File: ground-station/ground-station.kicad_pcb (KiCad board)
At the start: 2 copper layers, 61.6 x 32.6 mm, 53 parts, among them J1 Conn_01x02, J10 Conn_01x02, J2 Conn_01x02, J3 Conn_01x02, J4 Conn_01x02, J5 Conn_01x05, J6 Conn_01x04, J7 USB_B_Micro, J8 Conn_01x02, J9 Conn_01x02, SW1 SW_Push, U1 LM3940, U2 STM32F401RETx, U3 RFM69HCW

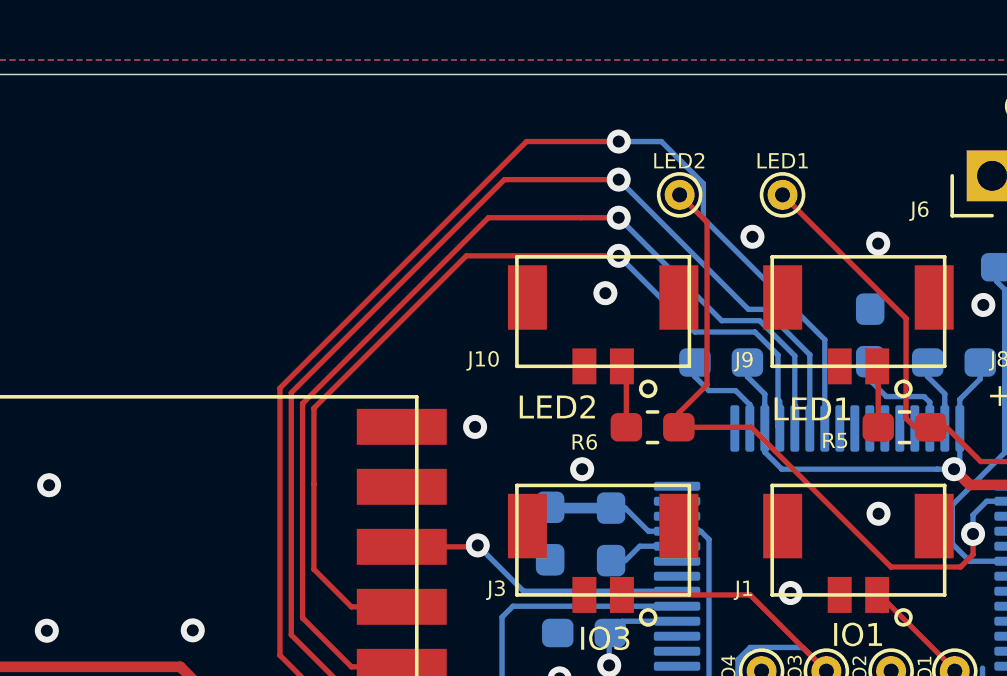
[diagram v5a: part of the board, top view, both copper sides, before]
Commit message: slight adjustments to increase ground plane
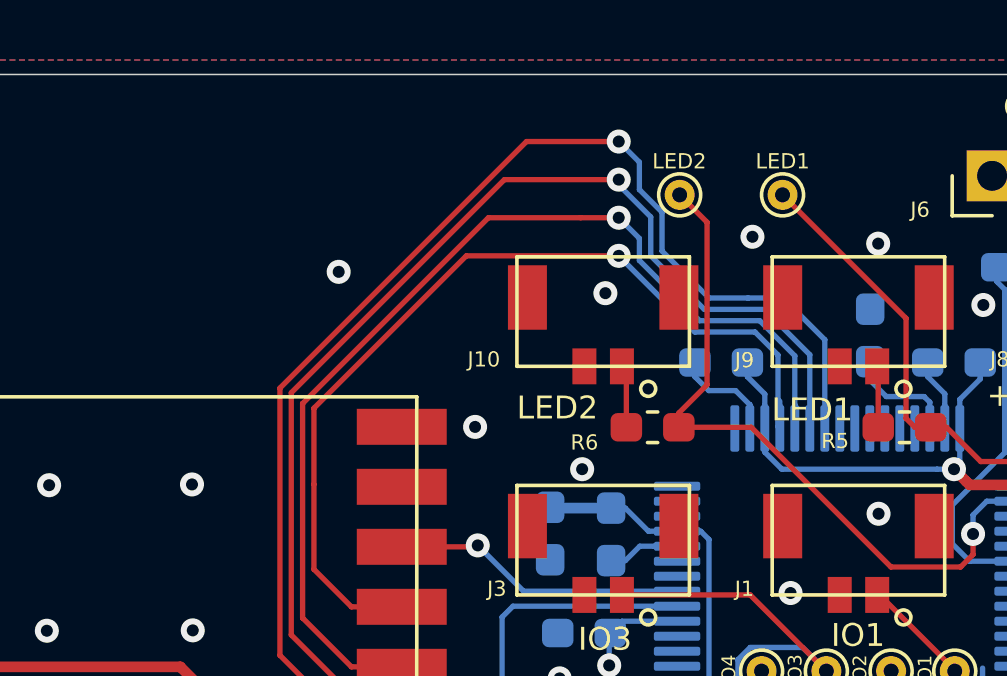
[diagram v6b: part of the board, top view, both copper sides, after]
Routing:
- net RadioMISO: track 44.7 -> 45.6 mm
- net RadioMOSI: track 41.9 -> 42.5 mm
- net GND: vias 37 -> 39
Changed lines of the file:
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@@
-(kicad_pcb (version 20171130) (host pcbnew "(5.1.5-0-10_14)")
+(kicad_pcb (version 20171130) (host pcbnew "(5.1.5)-3")
   (general
     (thickness 1.6)
     (drawings 39)
-    (tracks 435)
+    (tracks 444)
     (zones 0)
     (modules 53)
@@
   (page A4)
   (layers
-    (0 F.Cu signal hide)
+    (0 F.Cu signal)
     (31 B.Cu signal)
     (32 B.Adhes user)
@@
     (solder_mask_min_width 0.25)
     (aux_axis_origin 0 0)
-    (visible_elements FFFFFF7F)
+    (visible_elements 7FFFFFFF)
     (pcbplotparams
       (layerselection 0x010fc_ffffffff)
@@
   (gr_circle (center 219.329 52.832) (end 219.329 55.753) (layer B.CrtYd) (width 0.05))
   (gr_circle (center 219.329 52.832) (end 219.329 55.753) (layer F.CrtYd) (width 0.05))
+  (via (at 180.086 36.83) (size 0.8) (drill 0.4) (layers F.Cu B.Cu) (net 2))
+  (via (at 184.9755 29.7434) (size 0.8) (drill 0.4) (layers F.Cu B.Cu) (net 2))
   (segment (start 164.717 40.132) (end 163.322 40.132) (width 0.1778) (layer F.Cu) (net 1))
   (segment (start 170.121482 34.91) (end 172.078 34.91) (width 2.032) (layer F.Cu) (net 1))
@@
   (segment (start 189.563 38.91) (end 189.611 38.862) (width 0.1778) (layer F.Cu) (net 31))
   (segment (start 187.078 38.91) (end 189.563 38.91) (width 0.1778) (layer F.Cu) (net 31))
+  (segment (start 194.31 25.4) (end 194.31 25.4) (width 0.1778) (layer F.Cu) (net 32))
+  (segment (start 185.4002 44.91) (end 187.078 44.91) (width 0.1778) (layer F.Cu) (net 32))
+  (segment (start 183.016571 33.619125) (end 183.016572 42.526372) (width 0.1778) (layer F.Cu) (net 32))
+  (segment (start 183.016572 42.526372) (end 185.4002 44.91) (width 0.1778) (layer F.Cu) (net 32))
+  (segment (start 191.235696 25.4) (end 183.016571 33.619125) (width 0.1778) (layer F.Cu) (net 32))
+  (segment (start 194.31 25.4) (end 191.235696 25.4) (width 0.1778) (layer F.Cu) (net 32))
+  (segment (start 201.18 34.965) (end 201.18 32.006874) (width 0.1778) (layer B.Cu) (net 32))
+  (via (at 194.31 25.4) (size 0.8) (drill 0.4) (layers F.Cu B.Cu) (net 32))
+  (segment (start 199.789698 30.616572) (end 198.612998 30.616572) (width 0.1778) (layer B.Cu) (net 32))
+  (segment (start 201.18 32.006874) (end 199.789698 30.616572) (width 0.1778) (layer B.Cu) (net 32))
+  (segment (start 194.998901 27.002475) (end 195.754519 27.758095) (width 0.1778) (layer B.Cu) (net 32))
+  (segment (start 194.31 25.4) (end 194.998901 26.088901) (width 0.1778) (layer B.Cu) (net 32))
+  (segment (start 194.998901 26.088901) (end 194.998901 27.002475) (width 0.1778) (layer B.Cu) (net 32))
+  (segment (start 195.754519 29.051607) (end 197.319484 30.616572) (width 0.1778) (layer B.Cu) (net 32))
+  (segment (start 195.754519 27.758095) (end 195.754519 29.051607) (width 0.1778) (layer B.Cu) (net 32))
+  (segment (start 197.319484 30.616572) (end 198.628 30.616572) (width 0.1778) (layer B.Cu) (net 32))
   (via (at 194.31 26.67) (size 0.8) (drill 0.4) (layers F.Cu B.Cu) (net 33))
   (segment (start 187.078 46.91) (end 186.016674 46.91) (width 0.1778) (layer F.Cu) (net 33))
@@
   (segment (start 188.866901 44.078879) (end 188.586923 43.798901) (width 0.1778) (layer F.Cu) (net 33))
   (segment (start 187.078 46.91) (end 187.978 46.91) (width 0.1778) (layer F.Cu) (net 33))
-  (segment (start 194.31 25.4) (end 194.31 25.4) (width 0.1778) (layer F.Cu) (net 32))
-  (via (at 194.31 25.4) (size 0.8) (drill 0.4) (layers F.Cu B.Cu) (net 32))
-  (segment (start 185.4002 44.91) (end 187.078 44.91) (width 0.1778) (layer F.Cu) (net 32))
-  (segment (start 183.016571 33.619125) (end 183.016572 42.526372) (width 0.1778) (layer F.Cu) (net 32))
-  (segment (start 183.016572 42.526372) (end 185.4002 44.91) (width 0.1778) (layer F.Cu) (net 32))
-  (segment (start 191.235696 25.4) (end 183.016571 33.619125) (width 0.1778) (layer F.Cu) (net 32))
-  (segment (start 194.31 25.4) (end 191.235696 25.4) (width 0.1778) (layer F.Cu) (net 32))
-  (segment (start 195.731574 25.4) (end 194.875685 25.4) (width 0.1778) (layer B.Cu) (net 32))
-  (segment (start 197.130901 26.799327) (end 195.731574 25.4) (width 0.1778) (layer B.Cu) (net 32))
-  (segment (start 197.130901 27.957775) (end 197.130901 26.799327) (width 0.1778) (layer B.Cu) (net 32))
-  (segment (start 201.18 32.006874) (end 197.130901 27.957775) (width 0.1778) (layer B.Cu) (net 32))
-  (segment (start 194.875685 25.4) (end 194.31 25.4) (width 0.1778) (layer B.Cu) (net 32))
-  (segment (start 201.18 34.965) (end 201.18 32.006874) (width 0.1778) (layer B.Cu) (net 32))
   (segment (start 185.346879 43.798901) (end 183.394381 41.846403) (width 0.1778) (layer F.Cu) (net 33))
   (segment (start 183.394381 41.846403) (end 183.394381 33.775619) (width 0.1778) (layer F.Cu) (net 33))
@@
   (segment (start 190.5 26.67) (end 194.31 26.67) (width 0.1778) (layer F.Cu) (net 33))
   (segment (start 183.394381 33.775619) (end 190.5 26.67) (width 0.1778) (layer F.Cu) (net 33))
-  (segment (start 194.31 26.67) (end 198.634382 30.994382) (width 0.1778) (layer B.Cu) (net 33))
-  (segment (start 200.68 34.19) (end 200.68 34.965) (width 0.1778) (layer B.Cu) (net 33))
-  (segment (start 200.68 32.507934) (end 200.68 34.19) (width 0.1778) (layer B.Cu) (net 33))
-  (segment (start 199.166448 30.994382) (end 200.68 32.507934) (width 0.1778) (layer B.Cu) (net 33))
-  (segment (start 198.634382 30.994382) (end 199.166448 30.994382) (width 0.1778) (layer B.Cu) (net 33))
+  (segment (start 194.31 26.847878) (end 194.31 26.67) (width 0.1778) (layer B.Cu) (net 33))
+  (segment (start 195.37671 27.914588) (end 194.31 26.847878) (width 0.1778) (layer B.Cu) (net 33))
+  (segment (start 200.68 34.965) (end 200.68 32.507934) (width 0.1778) (layer B.Cu) (net 33))
+  (segment (start 200.68 32.507934) (end 199.166448 30.994382) (width 0.1778) (layer B.Cu) (net 33))
+  (segment (start 199.166448 30.994382) (end 197.16299 30.994382) (width 0.1778) (layer B.Cu) (net 33))
+  (segment (start 195.376711 29.208103) (end 195.37671 27.914588) (width 0.1778) (layer B.Cu) (net 33))
+  (segment (start 197.16299 30.994382) (end 195.376711 29.208103) (width 0.1778) (layer B.Cu) (net 33))
   (via (at 194.31 27.94) (size 0.8) (drill 0.4) (layers F.Cu B.Cu) (net 34))
   (segment (start 187.094 42.926) (end 187.078 42.91) (width 0.1778) (layer F.Cu) (net 34))
@@
   (segment (start 183.77219 34.133506) (end 189.965696 27.94) (width 0.1778) (layer F.Cu) (net 34))
   (segment (start 193.04 27.94) (end 194.31 27.94) (width 0.1778) (layer F.Cu) (net 34))
-  (segment (start 194.31 27.94) (end 197.74219 31.37219) (width 0.1778) (layer B.Cu) (net 34))
   (segment (start 200.18 34.175352) (end 200.18 34.19) (width 0.1778) (layer B.Cu) (net 34))
-  (segment (start 199.009953 31.372191) (end 200.18 32.542238) (width 0.1778) (layer B.Cu) (net 34))
   (segment (start 200.18 34.19) (end 200.18 34.965) (width 0.1778) (layer B.Cu) (net 34))
-  (segment (start 200.18 32.542238) (end 200.18 34.19) (width 0.1778) (layer B.Cu) (net 34))
-  (segment (start 197.74219 31.37219) (end 199.009953 31.372191) (width 0.1778) (layer B.Cu) (net 34))
+  (segment (start 200.18 32.542238) (end 199.009953 31.372191) (width 0.1778) (layer B.Cu) (net 34))
+  (segment (start 200.18 34.19) (end 200.18 32.542238) (width 0.1778) (layer B.Cu) (net 34))
+  (segment (start 199.009953 31.372191) (end 197.006494 31.37219) (width 0.1778) (layer B.Cu) (net 34))
+  (segment (start 194.998901 28.628901) (end 194.31 27.94) (width 0.1778) (layer B.Cu) (net 34))
+  (segment (start 194.998901 29.364597) (end 194.998901 28.628901) (width 0.1778) (layer B.Cu) (net 34))
+  (segment (start 197.006494 31.37219) (end 194.998901 29.364597) (width 0.1778) (layer B.Cu) (net 34))
   (segment (start 185.4002 40.91) (end 184.15 39.6598) (width 0.1778) (layer F.Cu) (net 35))
   (segment (start 184.15 36.83) (end 184.15 34.29) (width 0.1778) (layer F.Cu) (net 35))
@@
   (segment (start 199.68 34.19) (end 199.68 34.965) (width 0.1778) (layer B.Cu) (net 35))
   (segment (start 199.68 34.053172) (end 199.68 34.19) (width 0.1778) (layer B.Cu) (net 35))
-  (segment (start 196.85 31.75) (end 194.31 29.21) (width 0.1778) (layer B.Cu) (net 35))
   (segment (start 198.853458 31.75) (end 196.85 31.75) (width 0.1778) (layer B.Cu) (net 35))
   (segment (start 199.61891 32.515452) (end 198.853458 31.75) (width 0.1778) (layer B.Cu) (net 35))
   (segment (start 199.61891 34.90391) (end 199.61891 32.515452) (width 0.1778) (layer B.Cu) (net 35))
   (segment (start 199.68 34.965) (end 199.61891 34.90391) (width 0.1778) (layer B.Cu) (net 35))
+  (segment (start 196.85 31.75) (end 194.31 29.21) (width 0.1778) (layer B.Cu) (net 35))
   (zone (net 2) (net_name GND) (layer F.Cu) (hatch edge 0.508)
     (connect_pads (clearance 0.254))

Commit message: silkscreen and logos
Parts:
- added G***: LOGO, calstar_logos:star_8x7, F.Cu at (178.1, 27.2)
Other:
- board text added: "Ground Station v3.3"
